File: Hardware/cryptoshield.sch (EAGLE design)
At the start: 46 parts, among them J1 AVR_SPI_PRG_6PTH, Q1 BSS138, Q2 BSS138, Q3 BSS138, U1 74LVC1G04, U2 33mhz, U3 ID-12/20SMD, U4 ARDUINO_R3_SHIELD, U5 ATAES132, U6 AT97SC3204T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

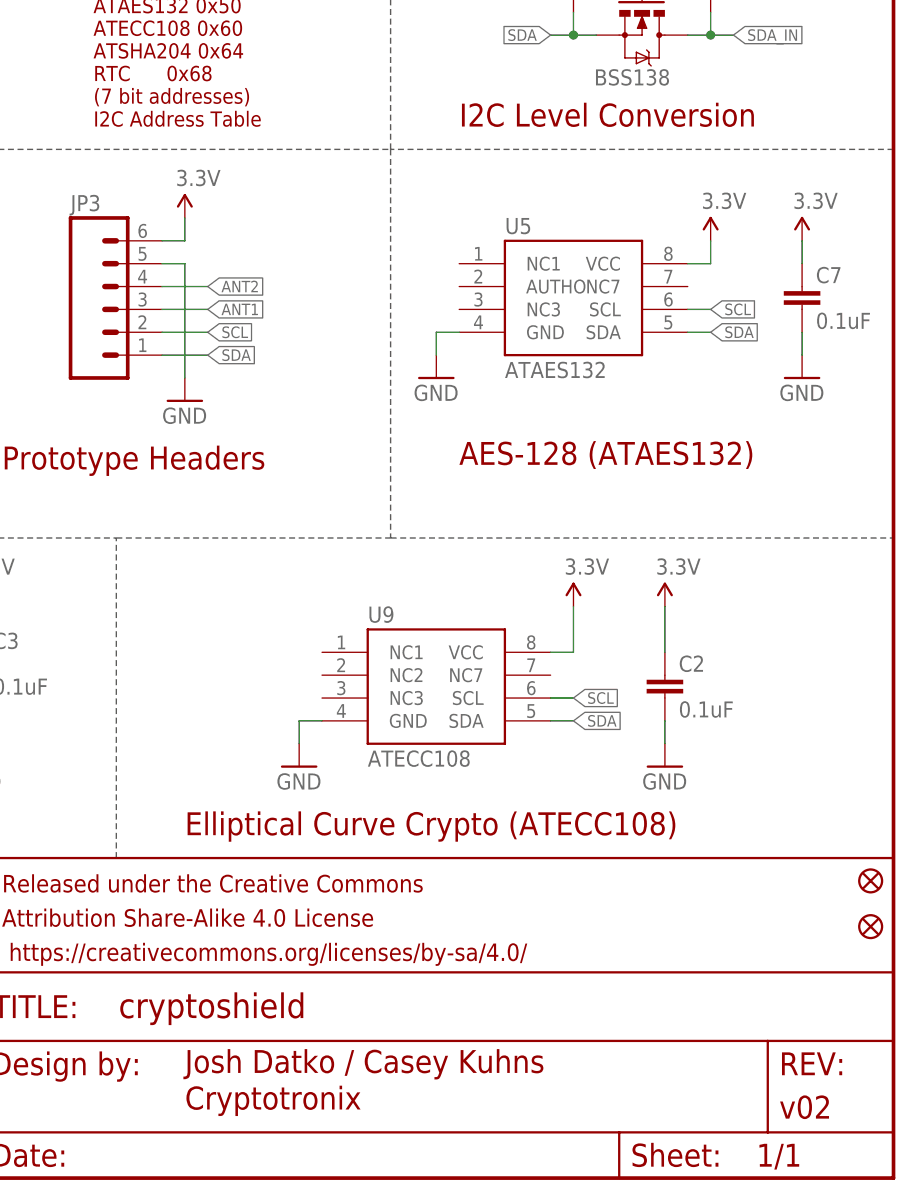
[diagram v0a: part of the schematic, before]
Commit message: Moved Stat Led away from board re-arranged proto area to conform with I2C standard layout flipped logos to match lable orientation
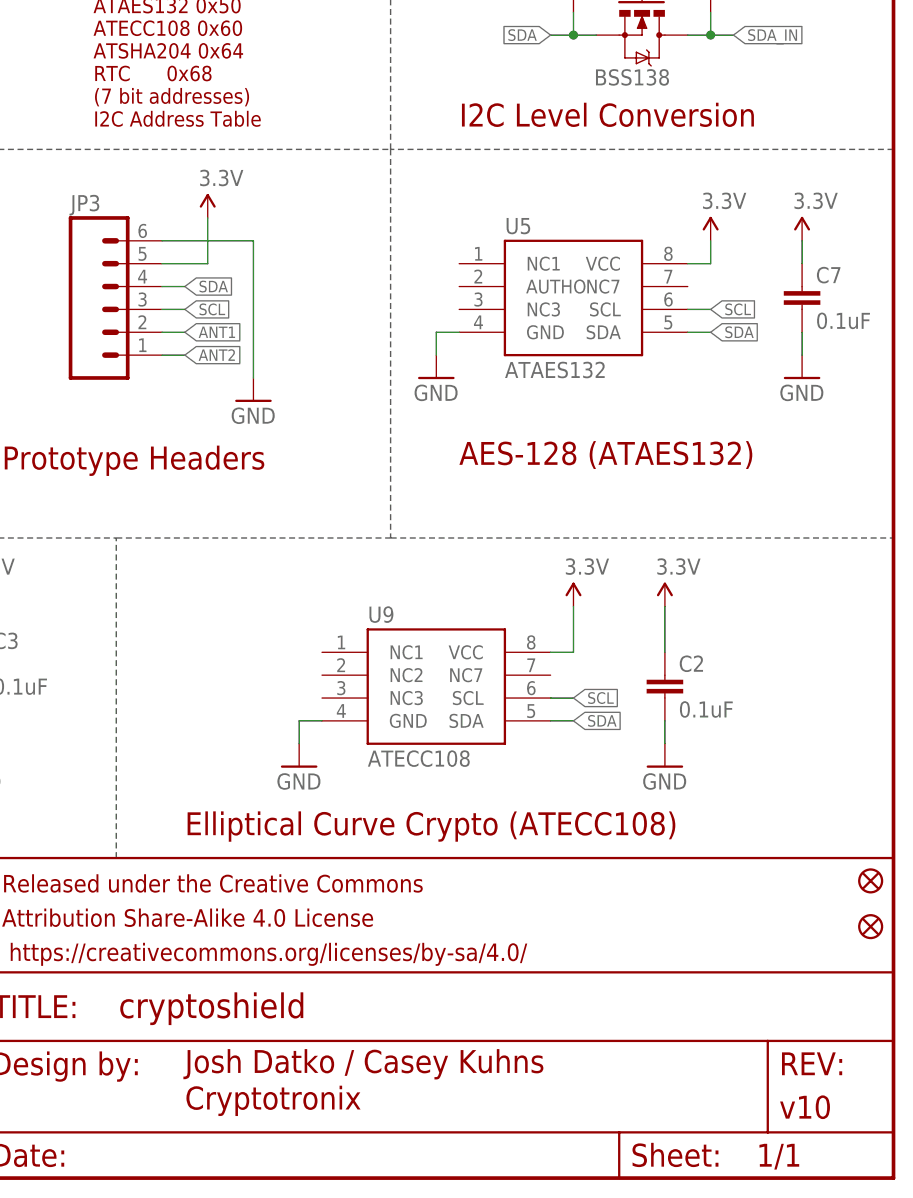
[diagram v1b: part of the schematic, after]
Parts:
- FRAME2: VERSION v02 -> v10
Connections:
- net 3.3V: now also JP3.5; no longer JP3.6
- net ANT1: now also JP3.2; no longer JP3.3
- net ANT2: now also JP3.1; no longer JP3.4
- net GND: now also JP3.6; no longer JP3.5
- net SCL: now also JP3.3; no longer JP3.2
- net SDA: now also JP3.4; no longer JP3.1
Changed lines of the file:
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@@
 <part name="GND6" library="SparkFun-Aesthetics" deviceset="GND" device=""/>
 <part name="JP1" library="SparkFun-Connectors" deviceset="M01" device="PTH"/>
-<part name="SUPPLY19" library="SparkFun-Aesthetics" deviceset="3.3V" device=""/>
 <part name="GND7" library="SparkFun-Aesthetics" deviceset="GND" device=""/>
 <part name="JP3" library="SparkFun-Connectors" deviceset="M06" device="NO_SILK_FEMALE_PTH"/>
@@
 <part name="FRAME2" library="SparkFun-Aesthetics" deviceset="FRAME-LETTER" device="">
 <attribute name="DESIGNER" value="Josh Datko / Casey Kuhns"/>
-<attribute name="VERSION" value="v02"/>
+<attribute name="VERSION" value="v10"/>
 </part>
 <part name="S2" library="SparkFun-Electromechanical" deviceset="SWITCH-MOMENTARY-2" device="SMD" value="Reset"/>
 <part name="LOGO2" library="SparkFun-Aesthetics" deviceset="OSHW-LOGO" device="S"/>
 <part name="LOGO3" library="SparkFun-Aesthetics" deviceset="SFE_LOGO_NAME_FLAME" device=".1_INCH"/>
+<part name="SUPPLY19" library="SparkFun-Aesthetics" deviceset="3.3V" device=""/>
 </parts>
 <sheets>
@@
 <attribute name="NAME" x="96.52" y="161.798" size="1.778" layer="95" rot="R180"/>
 </instance>
-<instance part="SUPPLY19" gate="G$1" x="170.18" y="106.68"/>
-<instance part="GND7" gate="1" x="170.18" y="86.36"/>
+<instance part="GND7" gate="1" x="177.8" y="86.36"/>
 <instance part="JP3" gate="G$1" x="162.56" y="96.52"/>
 <instance part="C13" gate="G$1" x="114.3" y="162.56" rot="MR0"/>
@@
 <instance part="LOGO2" gate="G$1" x="106.68" y="27.94"/>
 <instance part="LOGO3" gate="G$1" x="91.44" y="2.54"/>
+<instance part="SUPPLY19" gate="G$1" x="172.72" y="106.68"/>
 </instances>
 <busses>
@@
 </segment>
 <segment>
-<pinref part="GND7" gate="1" pin="GND"/>
-<wire x1="167.64" y1="101.6" x2="170.18" y2="101.6" width="0.1524" layer="91"/>
-<wire x1="170.18" y1="101.6" x2="170.18" y2="88.9" width="0.1524" layer="91"/>
-<pinref part="JP3" gate="G$1" pin="5"/>
-</segment>
-<segment>
 <pinref part="C13" gate="G$1" pin="2"/>
 <pinref part="GND8" gate="1" pin="GND"/>
@@
 <wire x1="116.84" y1="86.36" x2="119.38" y2="86.36" width="0.1524" layer="91"/>
 <wire x1="119.38" y1="86.36" x2="119.38" y2="83.82" width="0.1524" layer="91"/>
+</segment>
+<segment>
+<pinref part="JP3" gate="G$1" pin="6"/>
+<wire x1="167.64" y1="104.14" x2="177.8" y2="104.14" width="0.1524" layer="91"/>
+<wire x1="177.8" y1="104.14" x2="177.8" y2="88.9" width="0.1524" layer="91"/>
+<pinref part="GND7" gate="1" pin="GND"/>
 </segment>
 </net>
@@
 </segment>
 <segment>
-<wire x1="167.64" y1="93.98" x2="172.72" y2="93.98" width="0.1524" layer="91"/>
-<label x="172.72" y="93.98" size="1.27" layer="95" xref="yes"/>
-<pinref part="JP3" gate="G$1" pin="2"/>
+<pinref part="JP3" gate="G$1" pin="3"/>
+<wire x1="167.64" y1="96.52" x2="170.18" y2="96.52" width="0.1524" layer="91"/>
+<label x="170.18" y="96.52" size="1.27" layer="95" ratio="15" xref="yes"/>
 </segment>
 </net>
@@
 </segment>
 <segment>
-<wire x1="167.64" y1="91.44" x2="172.72" y2="91.44" width="0.1524" layer="91"/>
-<label x="172.72" y="91.44" size="1.27" layer="95" xref="yes"/>
-<pinref part="JP3" gate="G$1" pin="1"/>
+<pinref part="JP3" gate="G$1" pin="4"/>
+<wire x1="167.64" y1="99.06" x2="170.18" y2="99.06" width="0.1524" layer="91"/>
+<label x="170.18" y="99.06" size="1.27" layer="95" ratio="15" xref="yes"/>
 </segment>
 </net>
@@
 </segment>
 <segment>
-<wire x1="167.64" y1="104.14" x2="170.18" y2="104.14" width="0.1524" layer="91"/>
+<pinref part="JP3" gate="G$1" pin="5"/>
+<wire x1="167.64" y1="101.6" x2="172.72" y2="101.6" width="0.1524" layer="91"/>
+<wire x1="172.72" y1="101.6" x2="172.72" y2="106.68" width="0.1524" layer="91"/>
 <pinref part="SUPPLY19" gate="G$1" pin="3.3V"/>
-<wire x1="170.18" y1="106.68" x2="170.18" y2="104.14" width="0.1524" layer="91"/>
-<pinref part="JP3" gate="G$1" pin="6"/>
 </segment>
 </net>
@@
 </segment>
 <segment>
-<pinref part="JP3" gate="G$1" pin="3"/>
-<wire x1="167.64" y1="96.52" x2="172.72" y2="96.52" width="0.1524" layer="91"/>
-<label x="172.72" y="96.52" size="1.27" layer="95" xref="yes"/>
+<pinref part="JP3" gate="G$1" pin="2"/>
+<wire x1="167.64" y1="93.98" x2="170.18" y2="93.98" width="0.1524" layer="91"/>
+<label x="170.18" y="93.98" size="1.27" layer="95" ratio="15" xref="yes"/>
 </segment>
 </net>
@@
 </segment>
 <segment>
-<pinref part="JP3" gate="G$1" pin="4"/>
-<wire x1="167.64" y1="99.06" x2="172.72" y2="99.06" width="0.1524" layer="91"/>
-<label x="172.72" y="99.06" size="1.27" layer="95" xref="yes"/>
-</segment>
-</net>
+<pinref part="JP3" gate="G$1" pin="1"/>
+<wire x1="167.64" y1="91.44" x2="170.18" y2="91.44" width="0.1524" layer="91"/>
+<label x="170.18" y="91.44" size="1.27" layer="95" ratio="15" xref="yes"/>
+</segment>
+</net>
